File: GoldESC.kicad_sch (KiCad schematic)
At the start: 69 parts, among them J10 Conn_01x06, J30 CanOut, J80 DB15_Female_HighDensity, J81 Conn_02x07_Counter_Clockwise, J82 Conn_01x06, U2 DRV8300NIPWR, U30 MCP2551-I-SN, U31 CPDT-12V, U80 STM32F103C8Tx, U81 Crystal_GND3

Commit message: major schematic and pcb changes for production ready prototype
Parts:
- removed C85: 2.2uF, Capacitor_SMD:C_0603_1608Metric, symbol Device:C
- removed D70, D71, D72, D73, D74, D75, D76, D77: Z3V3, Diode_SMD:D_MiniMELF, symbol Device:D_Zener
- removed D80, D81: LED_Dual_AKA, LED_THT:LED_D3.0mm-3, symbol Device:LED_Dual_AKA
- removed J10: Conn_01x06, Connector_PinSocket_2.54mm:PinSocket_1x06_P2.54mm_Vertical, symbol Connector_Generic:Conn_01x06
- removed J80: DB15_Female_HighDensity, Connector_Dsub:DSUB-15-HD_Female_Horizontal_P2.29x1.98mm_EdgePinOffset3.03mm_Housed_MountingHolesOffset4.94mm, symbol Connector:DB15_Female_HighDensity
- removed L30: KCZ1210, AlfredoFootprints:KCZ1210, symbol Device:L_Coupled_1423
- removed R33: 120R?, Resistor_THT:R_Axial_DIN0207_L6.3mm_D2.5mm_P10.16mm_Horizontal, symbol Device:R
- removed R77: 2K2, Resistor_SMD:R_0603_1608Metric, symbol Device:R
- removed TP30, TP31, TP32, TP33, TP40, TP41, TP81: TestPoint, AlfredoFootprints:GE_TestPoint_Loop, symbol Connector:TestPoint
- added D70, D71, D72, D73: SM05T1G, Package_TO_SOT_SMD:SOT-23, symbol Diode:SM712_SOT23
- added D82, D84: LED_Green, LED_SMD:LED_0805_2012Metric, symbol Device:LED
- added D83, D85: LED_Red, LED_SMD:LED_0805_2012Metric, symbol Device:LED
- added J4: GND, AlfredoFootprints:GE_PwrPad1, symbol Connector_Generic:Conn_01x01
- added J5: DB15_Female_HighDensity, Connector_Dsub:DSUB-15-HD_Female_Horizontal_P2.29x1.98mm_EdgePinOffset3.03mm_Housed_MountingHolesOffset4.94mm, symbol Connector:DB15_Female_HighDensity
- added R4, R7: 1K, Resistor_SMD:R_0402_1005Metric, symbol Device:R
- C10: value 1uF -> 10uF,50V; footprint Capacitor_SMD:C_0805_2012Metric -> Capacitor_SMD:C_1206_3216Metric; LCSC ? -> C13585
- C4, C5, C6: footprint Capacitor_SMD:C_0603_1608Metric -> Capacitor_SMD:C_0402_1005Metric; LCSC C15849 -> C52923
- C42, C80: footprint Capacitor_SMD:C_0603_1608Metric -> Capacitor_SMD:C_0402_1005Metric; LCSC C14663 -> C307331
- C81, C82, C83, C84: footprint Capacitor_SMD:C_0603_1608Metric -> Capacitor_SMD:C_0402_1005Metric; LCSC C23630 -> (none)
- C88, C89: footprint Capacitor_SMD:C_0603_1608Metric -> Capacitor_SMD:C_0402_1005Metric; LCSC C1644 -> (none)
- D4, D5, D6: value CRH01 -> 1N58; footprint Diode_SMD:D_SOD-123F -> Diode_SMD:D_SOD-323_HandSoldering; LCSC C845528 -> C191023
- D42: value ZMM3V3 -> B3V3; footprint Diode_SMD:D_MiniMELF -> Diode_SMD:D_SOD-323_HandSoldering; LCSC C8056 -> C173439
- J81: footprint Connector_IDC:IDC-Header_2x07_P2.54mm_Vertical -> AlfredoFootprints:Connector_2x05_P1.27mm_IDC; symbol Connector_Generic:Conn_02x07_Odd_Even -> Connector_Generic:Conn_02x05_Odd_Even
- J82: value Conn_01x06 -> Conn_01x04; footprint Connector_PinSocket_2.54mm:PinSocket_1x06_P2.54mm_Vertical -> AlfredoFootprints:Connector_1x04_P1.27mm_SwdProg; symbol Connector_Generic:Conn_01x06 -> Connector_Generic:Conn_01x04
- R30: footprint Resistor_SMD:R_0603_1608Metric -> Resistor_SMD:R_0402_1005Metric; LCSC C23189 -> (none)
- R31, R40, R80: footprint Resistor_SMD:R_0603_1608Metric -> Resistor_SMD:R_0402_1005Metric; LCSC C25804 -> (none)
- R32: value 50K? -> 50K; footprint Resistor_THT:R_Axial_DIN0207_L6.3mm_D2.5mm_P10.16mm_Horizontal -> Resistor_SMD:R_0402_1005Metric
- R41: value 10K RTC -> 10K NTC; footprint Resistor_SMD:R_0603_1608Metric -> Resistor_SMD:R_0402_1005Metric; LCSC C95953 -> C77131
- R42, R70, R71, R72, R73, R74, R75, R76: footprint Resistor_SMD:R_0603_1608Metric -> Resistor_SMD:R_0402_1005Metric; LCSC C4190 -> (none)
- R43: footprint Resistor_SMD:R_0603_1608Metric -> Resistor_SMD:R_0402_1005Metric; LCSC C22809 -> (none)
- R81, R82: footprint Resistor_SMD:R_0603_1608Metric -> Resistor_SMD:R_0402_1005Metric; LCSC C23345 -> (none)
- R83, R84, R85, R86: footprint Resistor_SMD:R_0603_1608Metric -> Resistor_SMD:R_0402_1005Metric; LCSC C8218 -> (none)
- U2: value DRV8300NIPWR -> FD8288T (DRV8300); LCSC (none) -> C97683
- U80: value STM32F103C8Tx -> STM32F103CBTx; LCSC C8734 -> C8304
- U81: value Crystal_GND3 -> ABM3B-8.000MHZ
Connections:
- net +3V3: now also J81.1 (Pin_1), R4.1; no longer J81.3 (Pin_3)
- net +5V: now also C10.1, D4.2 (A), D5.2 (A), D6.2 (A), J81.2 (Pin_2), U2.7 (GVDD); no longer J81.1 (Pin_1), J82.6 (Pin_6)
- net CAN_H: now also U30.7 (CANH)
- net CAN_L: now also U30.6 (CANL)
- net GND: now also J81.3 (Pin_3), D70.3 (common), D71.3 (common), D72.3 (common), D73.3 (common), D82.1 (K), D83.1 (K), D84.1 (K), D85.1 (K), J4.1 (Pin_1), R7.2; no longer J81.5 (Pin_5), J81.7 (Pin_7), J82.5 (Pin_5)
- net QuadA: now also D70.2 (A2); no longer J81.2 (Pin_2), U80.17 (PA7)
- net QuadB: now also D70.1 (A1); no longer J81.4 (Pin_4), U80.19 (PB1)
- net VDD: no longer C10.1, D4.2 (A), D5.2 (A), D6.2 (A), U2.7 (GVDD)
- net at R83.1: now also D82.2 (A)
- net at R84.1: now also D83.2 (A)
- net at R86.1: now also D85.2 (A)
- net at R85.1: now also D84.2 (A)
- removed net Limit1A: J81.11 (Pin_11), R75.1, U80.39 (PB3)
- removed net Limit1B: J81.10 (Pin_10), R76.1, U80.40 (PB4)
- net Limit1C renamed LimitC
- net LimitC: now also J81.8 (Pin_8), D72.1 (A1); no longer J81.9 (Pin_9)
- removed net Limit2A: J81.13 (Pin_13), R73.1, U80.42 (PB6)
- net Limit2B renamed LimitE
- net LimitE: now also J81.9 (Pin_9), R76.1, D73.1 (A1); no longer J81.14 (Pin_14)
- removed net Limit2C: J81.12 (Pin_12), R72.1, U80.38 (PA15)
- net USB_DM renamed QuadB_USBDM
- net QuadB_USBDM: now also J81.5 (Pin_5); no longer J81.8 (Pin_8)
- net USB_DP renamed LimitB
- net LimitB: now also R73.1, U80.40 (PB4), D71.2 (A2); no longer R82.2
- new net GE-Fets-A/REF_1V65: R4.2, R7.1
- new net LimitA: D71.1 (A1), J81.4 (Pin_4), R72.1, U80.39 (PB3)
- new net LimitD: D72.2 (A2), J81.10 (Pin_10), R75.1, U80.42 (PB6)
- new net QuadA_USBDP: J81.7 (Pin_7), R82.2
- no-connect marks 1 -> 8
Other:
- sheet GE-Fets-A ports: added REF_1V65; removed none
- sheet GE-Fets-B ports: added REF_1V65; removed none
- sheet GE-Fets-C ports: added REF_1V65; removed none
- note added: "Vin max = 18V done: switch to LDR 3v3 reg? add TVS diodes change connector new leds change boot0 ckt to allow usb bootloader rethink C10? rethink bulk caps? rething C1-C3? change 0603s to 0402s do I really need sVLT_x? (yes) pick smaller 3V3 Z_diodes"
- note removed: "breakouts testpoints"
- note removed: "change boot0 ckt to allow usb bootloader"
- note removed: "do I really need sVLT_x?"
- moved on the sheet: J30, R30, R31, R32, R70, R71, R72, R73, R74, R83, R84, R85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

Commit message: First rev of layout before routing
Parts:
- removed D70, D71, D72, D73: SM05T1G, Package_TO_SOT_SMD:SOT-23, symbol Diode:SM712_SOT23
- removed R70, R71, R72, R73, R74, R75, R76: 2K2, Resistor_SMD:R_0402_1005Metric, symbol Device:R
- added D70, D71, D72, D73, D74, D75, D76: SD05, Diode_SMD:D_SOD-323, symbol Device:D_Zener
- C4, C5, C6: LCSC C52923 -> (none)
- C81, C82, C83, C84: LCSC (none) -> C12530
- C88, C89: LCSC (none) -> C1548
- D4, D5, D6: value 1N58 -> SDM20U40-7; footprint Diode_SMD:D_SOD-323_HandSoldering -> Diode_SMD:D_SOD-523; LCSC C191023 -> C139439
- D42: value B3V3 -> Z3V3; LCSC C173439 -> C75073
- J30: footprint AlfredoFootprints:TGD_ESC_SigPads -> AlfredoFootprints:GE_SigPad_1x02
- R4: value 1K -> 2K
- R40: value 10K -> 20K
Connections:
- net +3V3: no longer R4.1, R41.1
- net +5V: now also R4.1, R40.1
- net GND: now also R41.2; no longer R40.2
- net INHA: now also U80.31 (PA10); no longer U80.29 (PA8)
- net INHC: now also U80.29 (PA8); no longer U80.31 (PA10)
- net INLA: now also U80.28 (PB15); no longer U80.26 (PB13)
- net INLC: now also U80.26 (PB13); no longer U80.28 (PB15)
- net TEMP_FETS: now also R40.2, R41.1; no longer R40.1, R41.2
- no-connect marks 8 -> 7
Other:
- note added: "Vin max = 18V switch A and C phase parts done: switch to LDR 3v3 reg? add TVS diodes change connector new leds change boot0 ckt to allow usb bootloader rethink C10? rethink bulk caps? rething C1-C3? change 0603s to 0402s do I really need sVLT_x? (yes) pick smaller 3V3 Z_diodes"
- note removed: "Vin max = 18V done: switch to LDR 3v3 reg? add TVS diodes change connector new leds change boot0 ckt to allow usb bootloader rethink C10? rethink bulk caps? rething C1-C3? change 0603s to 0402s do I really need sVLT_x? (yes) pick smaller 3V3 Z_diodes"
- moved on the sheet: J5, R40, R41

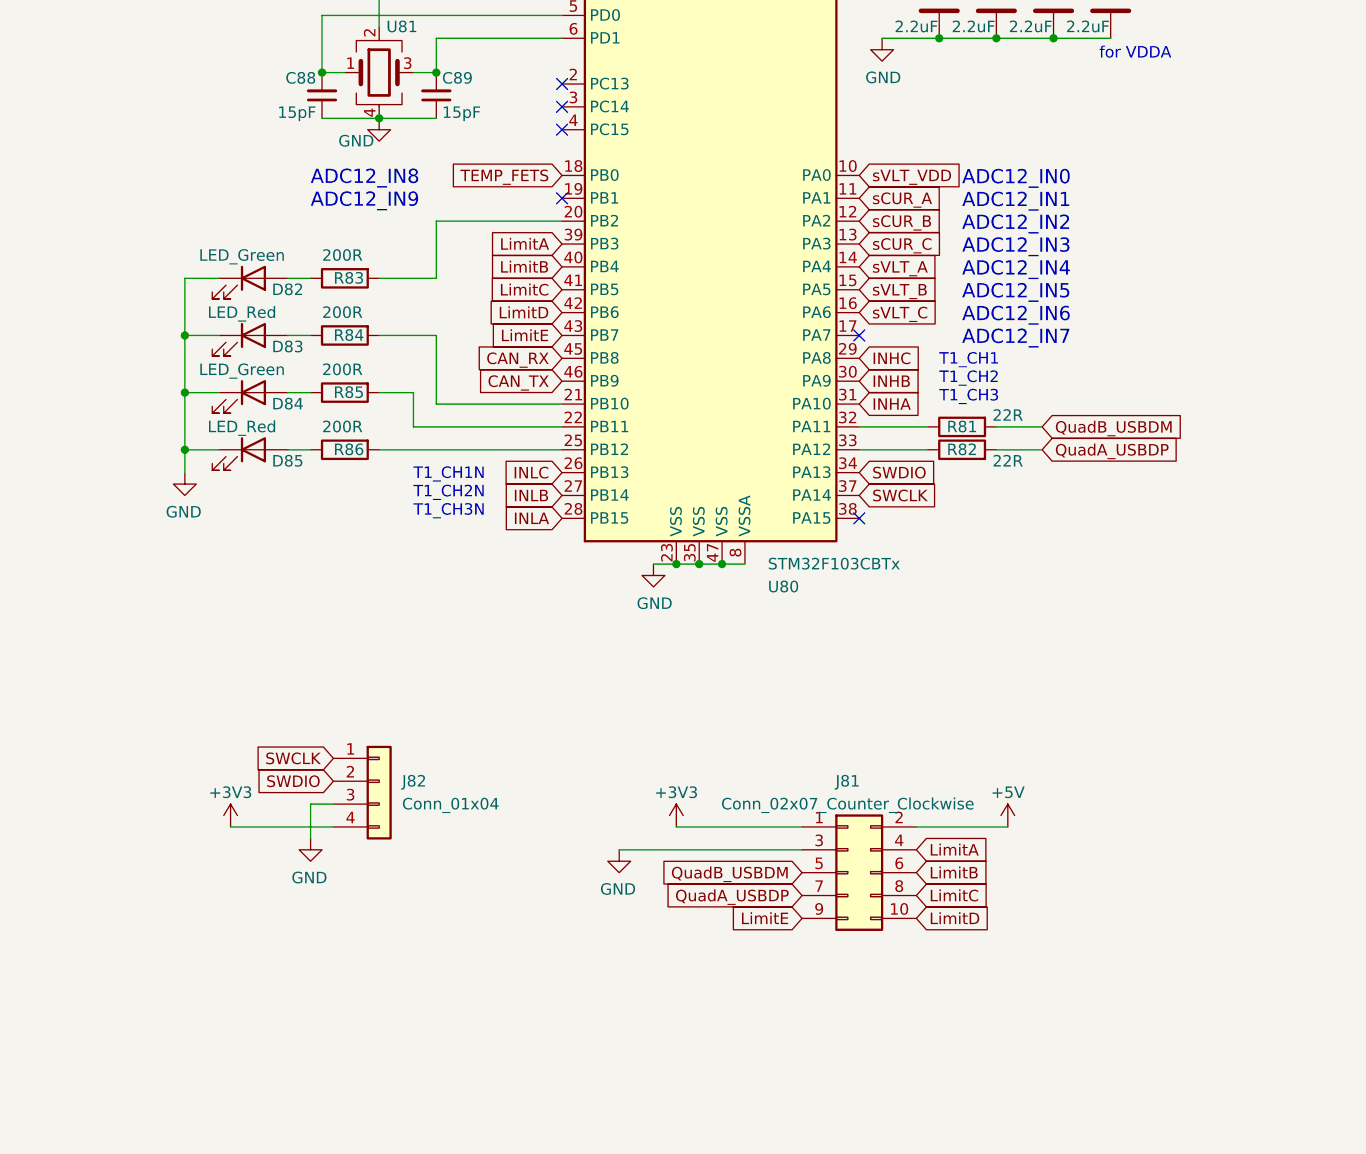
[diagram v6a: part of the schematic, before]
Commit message: all nets routed for next revision, no major drc errors
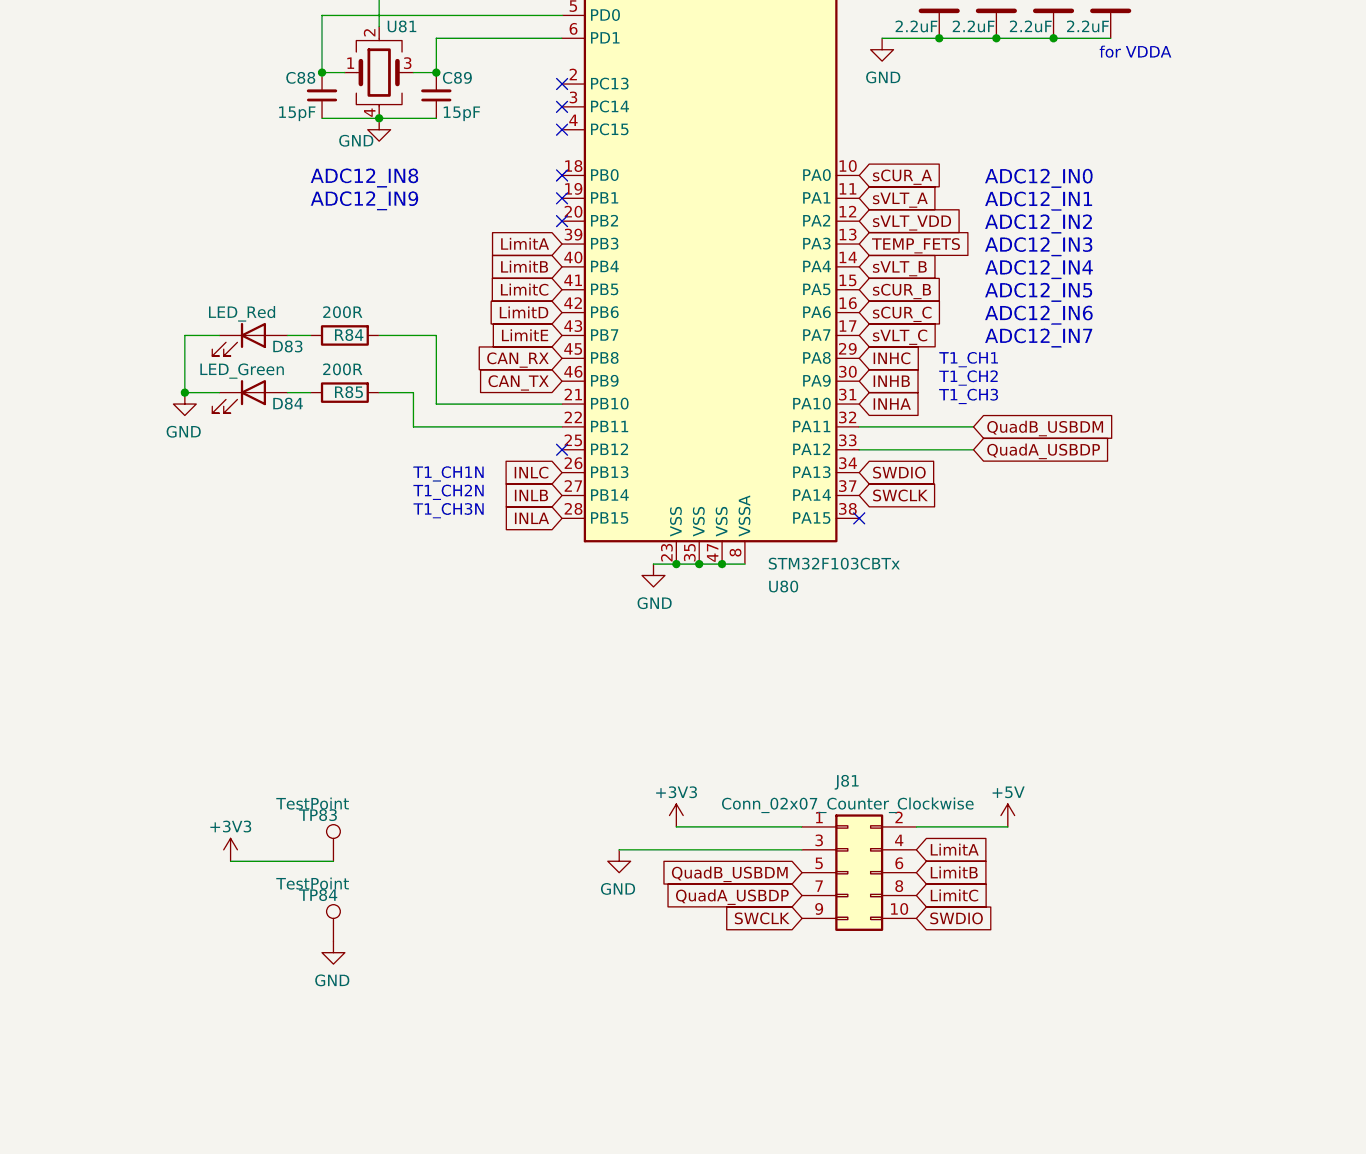
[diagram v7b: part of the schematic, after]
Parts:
- removed D82: LED_Green, LED_SMD:LED_0805_2012Metric, symbol Device:LED
- removed D85: LED_Red, LED_SMD:LED_0805_2012Metric, symbol Device:LED
- removed J82: Conn_01x04, AlfredoFootprints:Connector_1x04_P1.27mm_SwdProg, symbol Connector_Generic:Conn_01x04
- removed R81, R82: 22R, Resistor_SMD:R_0402_1005Metric, symbol Device:R
- removed R83, R86: 200R, Resistor_SMD:R_0402_1005Metric, symbol Device:R
- added TP83, TP84: TestPoint, AlfredoFootprints:GE_TestPoint_Loop, symbol Connector:TestPoint
- C4, C5, C6: LCSC (none) -> C52923
- R30: LCSC (none) -> C25908
- R31, R80: LCSC (none) -> C25744
- R32: LCSC (none) -> C166559
- R4: LCSC (none) -> C4109
- R40: LCSC (none) -> C25765
- R42: LCSC (none) -> C25879
- R43: LCSC (none) -> C25756
- R7: LCSC (none) -> C11702
- R84, R85: LCSC (none) -> C25087
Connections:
- net +3V3: now also TP83.1
- net GND: now also TP84.1
- net LimitD: no longer J81.10 (Pin_10)
- net LimitE: no longer J81.9 (Pin_9)
- net QuadA_USBDP: now also U80.33 (PA12)
- net QuadB_USBDM: now also U80.32 (PA11)
- net SWCLK: now also J81.9 (Pin_9)
- net SWDIO: now also J81.10 (Pin_10)
- net TEMP_FETS: now also U80.13 (PA3); no longer U80.18 (PB0)
- net sCUR_A: now also U80.10 (PA0); no longer U80.11 (PA1)
- net sCUR_B: now also U80.15 (PA5); no longer U80.12 (PA2)
- net sCUR_C: now also U80.16 (PA6); no longer U80.13 (PA3)
- net sVLT_A: now also U80.11 (PA1); no longer U80.14 (PA4)
- net sVLT_B: now also U80.14 (PA4); no longer U80.15 (PA5)
- net sVLT_C: now also U80.17 (PA7); no longer U80.16 (PA6)
- net sVLT_VDD: now also U80.12 (PA2); no longer U80.10 (PA0)
- no-connect marks 7 -> 9

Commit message: version for 9/10/22 jlc order
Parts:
- removed D70, D71, D72, D73, D74, D75, D76: SD05, Diode_SMD:D_SOD-323, symbol Device:D_Zener
- J81: LCSC (none) -> C2962225
- R32: value 50K -> 51K; LCSC C166559 -> C25794
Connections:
- net SWCLK: now also J81.10 (Pin_10); no longer J81.9 (Pin_9)
- net SWDIO: now also J81.9 (Pin_9); no longer J81.10 (Pin_10)
